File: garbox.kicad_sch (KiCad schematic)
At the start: 21 parts, among them J2 USB_Header, J5 SD_Header, J6 PowerBreakoutHeader, J7 BMS_Header, J8 Audio_Header, J9 GPIO_Header, SW1 RotaryEncoder, U1 ESP32-S3-WROOM-1-N4R8

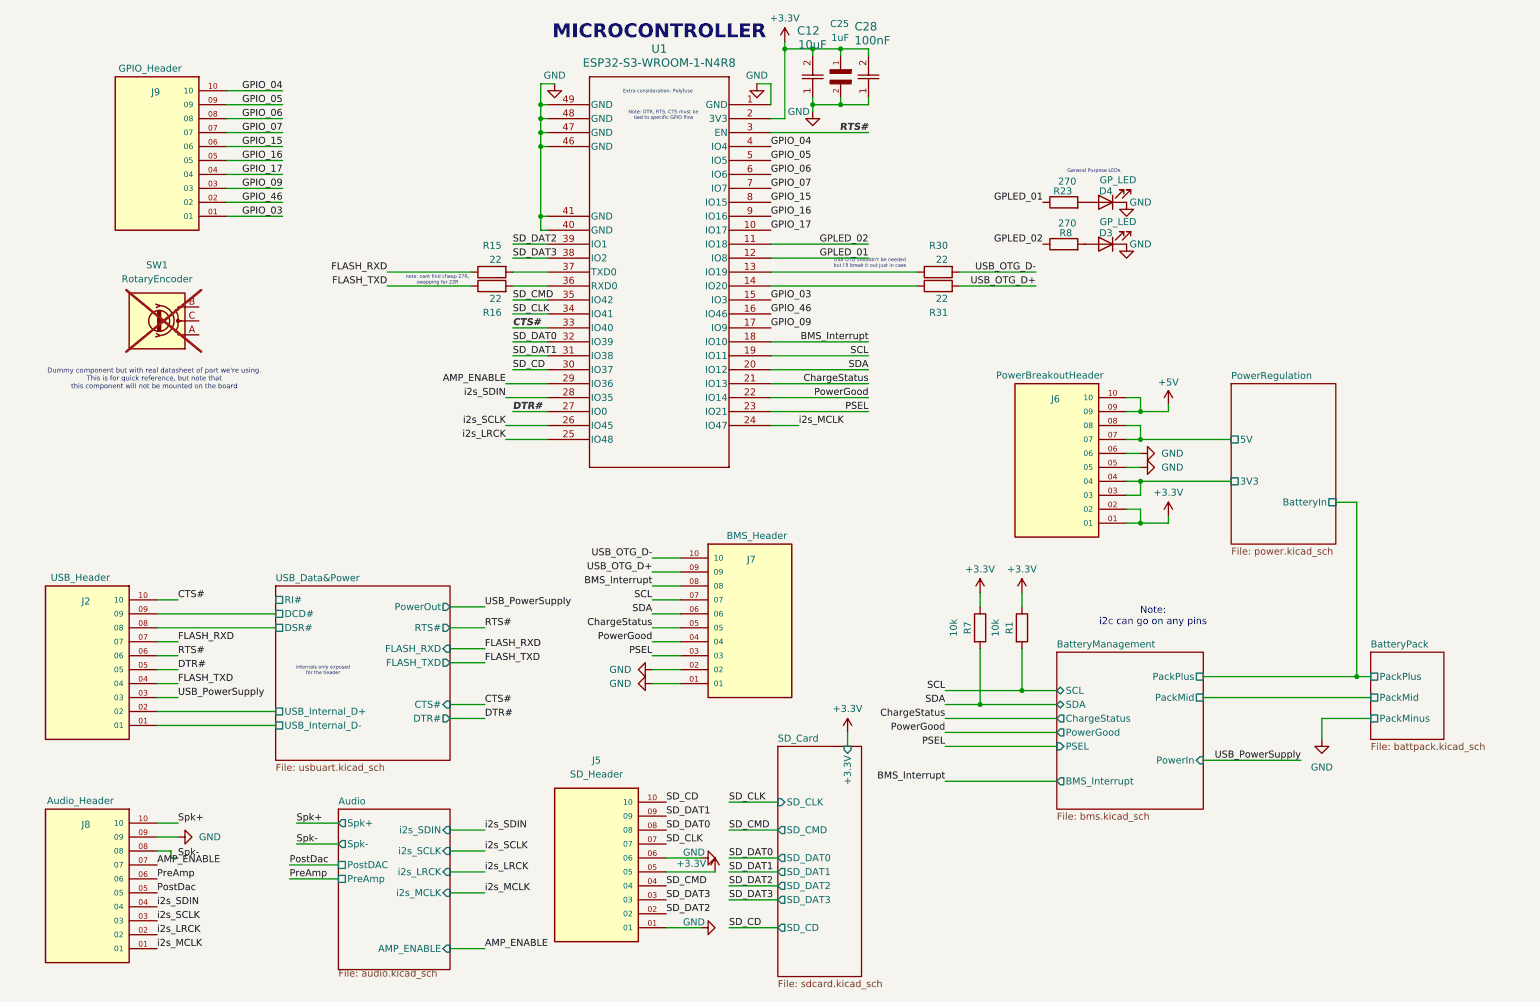
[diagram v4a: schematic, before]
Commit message: Updated part numbers
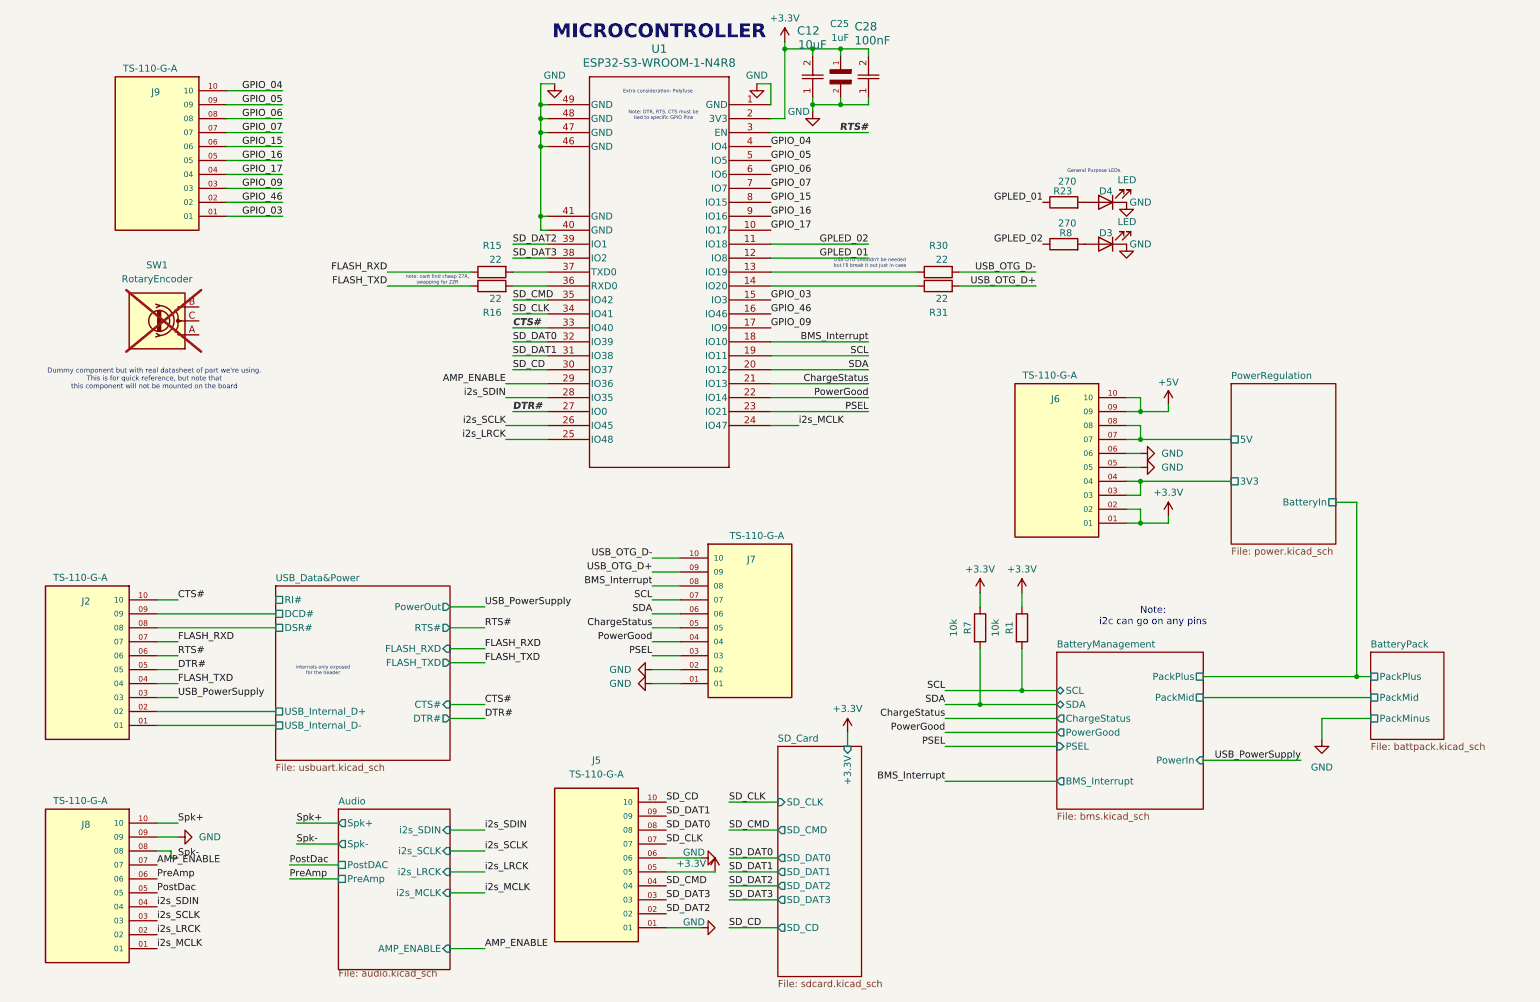
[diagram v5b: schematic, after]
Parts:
- D3, D4: value GP_LED -> LED
- J2: value USB_Header -> TS-110-G-A; MPN C3333064 -> C57369
- J5: value SD_Header -> TS-110-G-A
- J6: value PowerBreakoutHeader -> TS-110-G-A
- J7: value BMS_Header -> TS-110-G-A
- J8: value Audio_Header -> TS-110-G-A
- J9: value GPIO_Header -> TS-110-G-A
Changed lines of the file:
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@@
 			)
 		)
-		(property "Value" "Audio_Header"
+		(property "Value" "TS-110-G-A"
 			(at 25.4 159.766 0)
 			(effects
@@
 			)
 		)
-		(property "Description" "TS-110-G-A"
+		(property "Description" "Audio_Header"
 			(at 26.67 173.99 0)
 			(effects
@@
 			)
 		)
+		(property "FIX" ""
+			(at 26.67 173.99 0)
+			(effects
+				(font
+					(size 1.27 1.27)
+				)
+				(hide yes)
+			)
+		)
 		(pin "01"
 		)
@@
 			)
 		)
-		(property "Value" "USB_Header"
+		(property "Value" "TS-110-G-A"
 			(at 25.4 119.126 0)
 			(effects
@@
 			)
 		)
-		(property "Description" "TS-110-G-A"
+		(property "Description" "USB_Header"
 			(at 26.67 133.35 0)
 			(effects
@@
 			)
 		)
-		(property "MPN" "C3333064"
+		(property "MPN" "C57369"
+			(at 26.67 133.35 0)
+			(effects
+				(font
+					(size 1.27 1.27)
+				)
+				(hide yes)
+			)
+		)
+		(property "FIX" ""
 			(at 26.67 133.35 0)
 			(effects
@@
 			)
 		)
+		(property "FIX" ""
+			(at 181.61 63.5 90)
+			(effects
+				(font
+					(size 1.27 1.27)
+				)
+				(hide yes)
+			)
+		)
 		(pin "2"
 		)
@@
 			)
 		)
-		(property "Value" "PowerBreakoutHeader"
+		(property "Value" "TS-110-G-A"
 			(at 201.93 82.296 0)
 			(effects
@@
 			)
 		)
-		(property "Description" "TS-110-G-A"
+		(property "Description" "PowerBreakoutHeader"
 			(at 203.2 96.52 0)
 			(effects
@@
 			)
 		)
+		(property "FIX" ""
+			(at 203.2 96.52 0)
+			(effects
+				(font
+					(size 1.27 1.27)
+				)
+				(hide yes)
+			)
+		)
 		(pin "01"
 		)
@@
 			)
 		)
+		(property "FIX" ""
+			(at 163.83 26.67 90)
+			(effects
+				(font
+					(size 1.27 1.27)
+				)
+				(hide yes)
+			)
+		)
 		(pin "2"
 		)
@@
 			)
 		)
-		(property "Value" "BMS_Header"
+		(property "Value" "TS-110-G-A"
 			(at 148.59 111.506 0)
 			(effects
@@
 			)
 		)
-		(property "Description" "TS-110-G-A"
+		(property "Description" "BMS_Header"
 			(at 147.32 125.73 0)
 			(effects
@@
 			)
 		)
+		(property "FIX" ""
+			(at 147.32 125.73 0)
+			(effects
+				(font
+					(size 1.27 1.27)
+				)
+				(hide yes)
+			)
+		)
 		(pin "01"
 		)
@@
 			)
 		)
+		(property "FIX" ""
+			(at 100.33 66.04 90)
+			(effects
+				(font
+					(size 1.27 1.27)
+				)
+				(hide yes)
+			)
+		)
 		(pin "2"
 		)
@@
 			)
 		)
+		(property "FIX" ""
+			(at 204.47 50.8 90)
+			(effects
+				(font
+					(size 1.27 1.27)
+				)
+				(hide yes)
+			)
+		)
 		(pin "2"
 		)
@@
 			)
 		)
+		(property "FIX" ""
+			(at 181.61 66.04 90)
+			(effects
+				(font
+					(size 1.27 1.27)
+				)
+				(hide yes)
+			)
+		)
 		(pin "2"
 		)
@@
 			)
 		)
+		(property "FIX" ""
+			(at 39.37 72.39 0)
+			(effects
+				(font
+					(size 1.27 1.27)
+				)
+				(hide yes)
+			)
+		)
 		(pin "B"
 		)
@@
 			)
 		)
+		(property "FIX" ""
+			(at 189.23 128.27 90)
+			(effects
+				(font
+					(size 1.27 1.27)
+				)
+				(hide yes)
+			)
+		)
 		(pin "2"
 		)
@@
 			)
 		)
-		(property "Value" "SD_Header"
+		(property "Value" "TS-110-G-A"
 			(at 119.38 154.94 0)
 			(effects
@@
 			)
 		)
-		(property "Description" "TS-110-G-A"
+		(property "Description" "SD_Header"
 			(at 119.38 170.18 0)
 			(effects
@@
 			)
 		)
+		(property "FIX" ""
+			(at 119.38 170.18 0)
+			(effects
+				(font
+					(size 1.27 1.27)
+				)
+				(hide yes)
+			)
+		)
 		(pin "01"
 		)
@@
 			)
 		)
-		(property "Value" "GP_LED"
+		(property "Value" "LED"
 			(at 217.678 46.736 0)
 			(effects
@@
 			)
 		)
-		(property "Description" "Light emitting diode"
+		(property "Description" "Light emitting diode GP_LED"
 			(at 212.09 50.8 0)
 			(effects
@@
 			)
 		)
+		(property "FIX" ""
+			(at 212.09 50.8 0)
+			(effects
+				(font
+					(size 1.27 1.27)
+				)
+				(hide yes)
+			)
+		)
 		(pin "1"
 		)
@@
 			)
 		)
-		(property "Value" "GPIO_Header"
+		(property "Value" "TS-110-G-A"
 			(at 38.1 26.416 0)
 			(effects
@@
 			)
 		)
-		(property "Description" "TS-110-G-A"
+		(property "Description" "GPIO_Header"
 			(at 39.37 40.64 0)
 			(effects
@@
 			)
 		)
+		(property "FIX" ""
+			(at 39.37 40.64 0)
+			(effects
+				(font
+					(size 1.27 1.27)
+				)
+				(hide yes)
+			)
+		)
 		(pin "01"
 		)
@@
 			)
 		)
+		(property "FIX" ""
+			(at 158.75 31.75 90)
+			(effects
+				(font
+					(size 1.27 1.27)
+				)
+				(hide yes)
+			)
+		)
 		(pin "2"
 		)
@@
 			)
 		)
+		(property "FIX" ""
+			(at 168.91 31.75 90)
+			(effects
+				(font
+					(size 1.27 1.27)
+				)
+				(hide yes)
+			)
+		)
 		(pin "2"
 		)
@@
 			)
 		)
+		(property "FIX" ""
+			(at 100.33 63.5 90)
+			(effects
+				(font
+					(size 1.27 1.27)
+				)
+				(hide yes)
+			)
+		)
 		(pin "2"
 		)
@@
 			)
 		)
+		(property "FIX" ""
+			(at 151.13 33.02 0)
+			(effects
+				(font
+					(size 1.27 1.27)
+				)
+				(hide yes)
+			)
+		)
 		(pin "39"
 		)
@@
 			)
 		)
+		(property "FIX" ""
+			(at 196.85 128.27 90)
+			(effects
+				(font
+					(size 1.27 1.27)
+				)
+				(hide yes)
+			)
+		)
 		(pin "2"
 		)
@@
 			)
 		)
+		(property "FIX" ""
+			(at 204.47 58.42 90)
+			(effects
+				(font
+					(size 1.27 1.27)
+				)
+				(hide yes)
+			)
+		)
 		(pin "2"
 		)
@@
 			)
 		)
-		(property "Value" "GP_LED"
+		(property "Value" "LED"
 			(at 217.678 54.356 0)
 			(effects
@@
 			)
 		)
-		(property "Description" "Light emitting diode"
+		(property "Description" "Light emitting diode GP_LED"
 			(at 212.09 58.42 0)
 			(effects
@@
 			(at 212.09 58.42 0)
 			(effects
+				(font
+					(size 1.27 1.27)
+				)
+				(hide yes)
+			)
+		)
+		(property "FIX" ""
+			(at 212.09 58.42 0)
+			(effects

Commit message: swapped esp32-s3-wroom-1-n4r8 for esp32-s3-wroom-1u-n4r8 board, fixed unconnected net on USB connector, and tidied up some traces on usb.
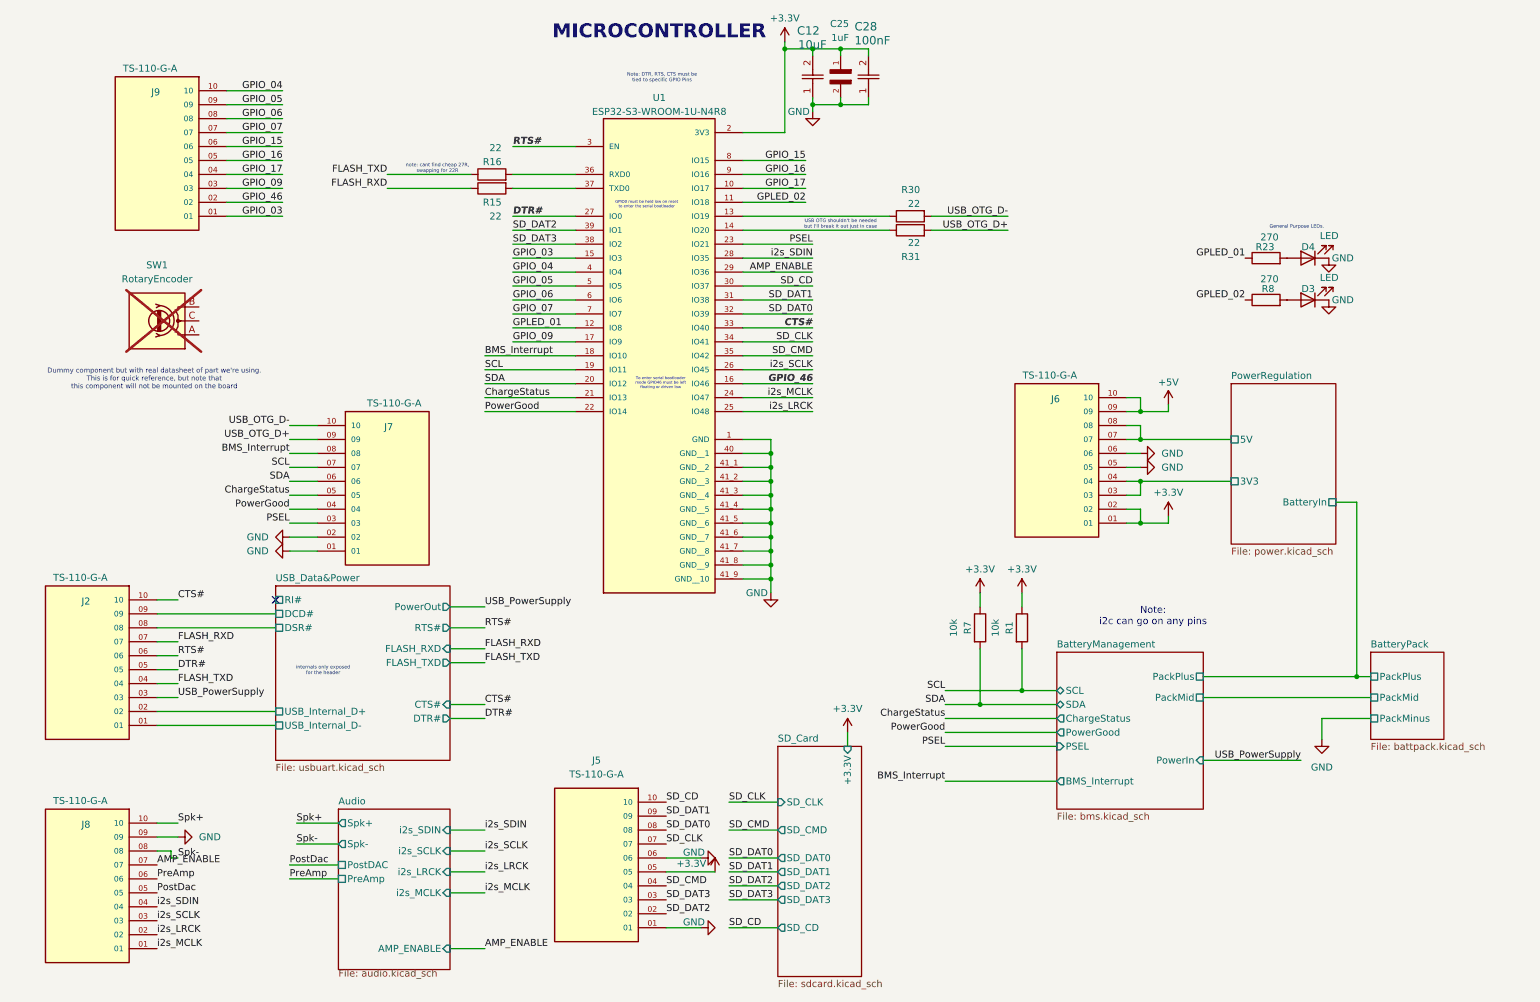
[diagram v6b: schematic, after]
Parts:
- removed U1: ESP32-S3-WROOM-1-N4R8, ESP32_S3_WROOM_1_N4R8:ESP32-S3-WROOM-1_EXP, symbol ESP32-S3-WROOM-1-N4R8:ESP32-S3-WROOM-1-N4R8
- added U1: ESP32-S3-WROOM-1U-N4R8, ESP32_S3_WROOM_1U_N4R8:XCVR_ESP32-S3-WROOM-1U-N4R8, symbol ESP32_S3_WROOM_1U_N4R8:ESP32-S3-WROOM-1U-N4R8
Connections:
- net +3.3V: now also U1.2 (3V3)
- net AMP_ENABLE: now also U1.29 (IO36)
- net BMS_Interrupt: now also U1.18 (IO10)
- net CTS#: now also U1.33 (IO40)
- net ChargeStatus: now also U1.21 (IO13)
- net DTR#: now also U1.27 (IO0)
- net GND: now also U1.1 (GND), U1.40 (GND__1), U1.41_1 (GND__2), U1.41_2 (GND__3), U1.41_3 (GND__4), U1.41_4 (GND__5), U1.41_5 (GND__6), U1.41_6 (GND__7), U1.41_7 (GND__8), U1.41_8 (GND__9), U1.41_9 (GND__10)
- net GPIO_03: now also U1.15 (IO3)
- net GPIO_04: now also U1.4 (IO4)
- net GPIO_05: now also U1.5 (IO5)
- net GPIO_06: now also U1.6 (IO6)
- net GPIO_07: now also U1.7 (IO7)
- net GPIO_09: now also U1.17 (IO9)
- net GPIO_15: now also U1.8 (IO15)
- net GPIO_16: now also U1.9 (IO16)
- net GPIO_17: now also U1.10 (IO17)
- net GPIO_46: now also U1.16 (IO46)
- net GPLED_01: now also U1.12 (IO8)
- net GPLED_02: now also U1.11 (IO18)
- net PSEL: now also U1.23 (IO21)
- net PowerGood: now also U1.22 (IO14)
- net RTS#: now also U1.3 (EN)
- net SCL: now also U1.19 (IO11)
- net SDA: now also U1.20 (IO12)
- net SD_CD: now also U1.30 (IO37)
- net SD_CLK: now also U1.34 (IO41)
- net SD_CMD: now also U1.35 (IO42)
- net SD_DAT0: now also U1.32 (IO39)
- net SD_DAT1: now also U1.31 (IO38)
- net SD_DAT2: now also U1.39 (IO1)
- net SD_DAT3: now also U1.38 (IO2)
- net i2s_LRCK: now also U1.25 (IO48)
- net i2s_MCLK: now also U1.24 (IO47)
- net i2s_SCLK: now also U1.26 (IO45)
- net i2s_SDIN: now also U1.28 (IO35)
- net at R30.1: now also U1.13 (IO19)
- net at R16.2: now also U1.36 (RXD0)
- net at R31.1: now also U1.14 (IO20)
- net at R15.2: now also U1.37 (TXD0)
- no-connect marks 0 -> 1
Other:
- note added: "GPIO0 must be held low on reset to enter the serial bootloader"
- note added: "To enter serial bootloader mode GPIO46 must be left floating or driven low"
- note removed: "Extra consideration: Polyfuse"
- moved on the sheet: D3, D4, J7, R15, R16, R23, R30, R31, R8
